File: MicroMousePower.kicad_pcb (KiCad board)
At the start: 2 copper layers, 103 parts, among them J1 USB_C_Receptacle_PowerOnly_6P, J2 Conn_02x16_Odd_Even, J3 Conn_01x02_Pin, Q1 TIP41C, Q2 TIP41C, Q3 TIP41C, U1 INA219AxDCN, U2 MCP73831-3-MC, U3 CH224K, U4 DRV8833PWPR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

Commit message: try 2
try ?
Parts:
- moved D1 144.7 mm to (259.3, 51.6), turned to -90 degrees
- moved C15 130.1 mm to (248.5, 88.1), turned to 180 degrees
- moved C8 129.2 mm to (248.5, 91.4), turned to 180 degrees
- moved D2 128.2 mm to (248.0, 72.2), turned to -90 degrees
- moved R36 125.9 mm to (264.2, 112.9), turned to -90 degrees
- moved R19 124.8 mm to (256.8, 47.8), turned to 180 degrees
- moved R21 124.7 mm to (251.7, 47.8), turned to 180 degrees
- moved R25 124.6 mm to (258.2, 74.7)
- moved R12 121.9 mm to (252.0, 120.1)
- moved R26 121.5 mm to (263.1, 74.7)
- moved U8 120.9 mm to (250.7, 107.8)
- moved R38 118.0 mm to (258.7, 111.6), turned to 90 degrees
- moved R20 117.8 mm to (259.3, 58.9), turned to -90 degrees
- moved TP8 117.4 mm to (266.1, 102.7)
- moved R41 117.2 mm to (251.8, 126.3)
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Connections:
- TP18 pad 1: unconnected-(TP18-Pad1) -> /3V3
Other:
- board text added: "Vc"
- board text added: "Ve"

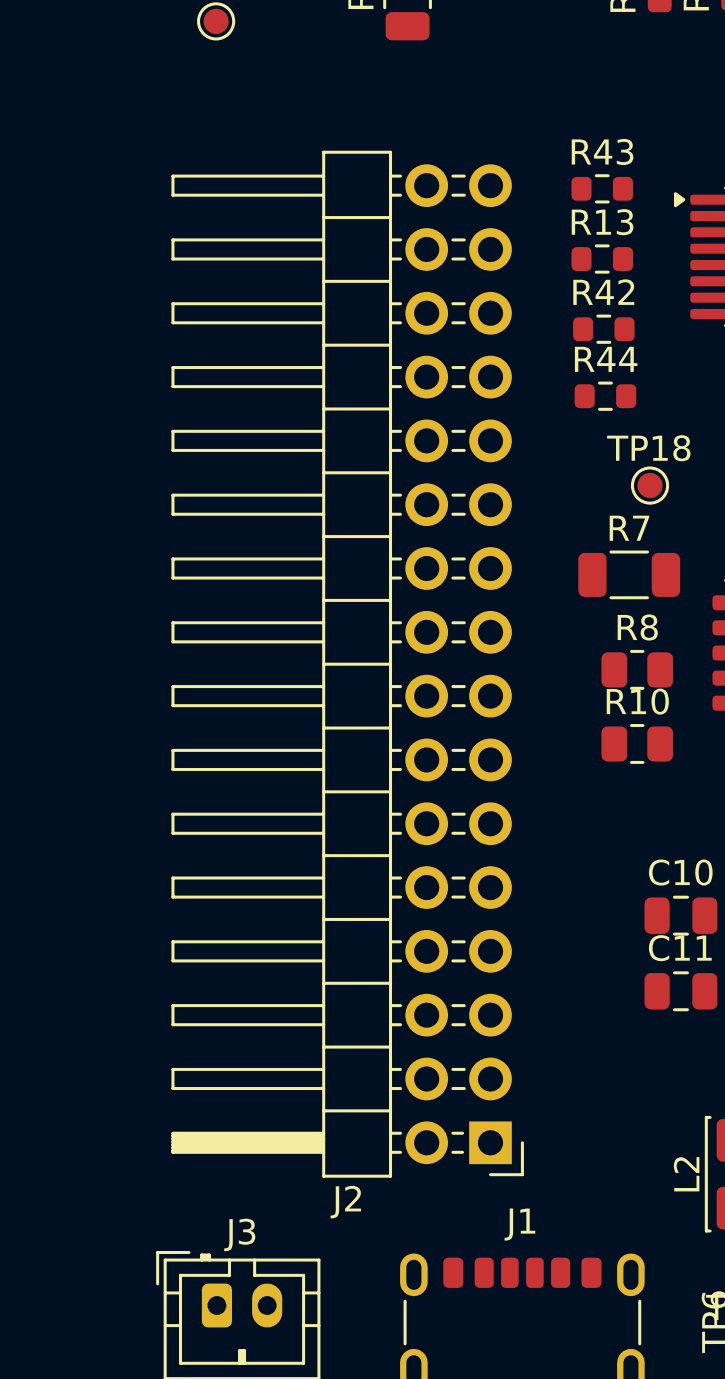
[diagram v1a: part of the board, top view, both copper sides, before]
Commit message: updated pinheader footprint
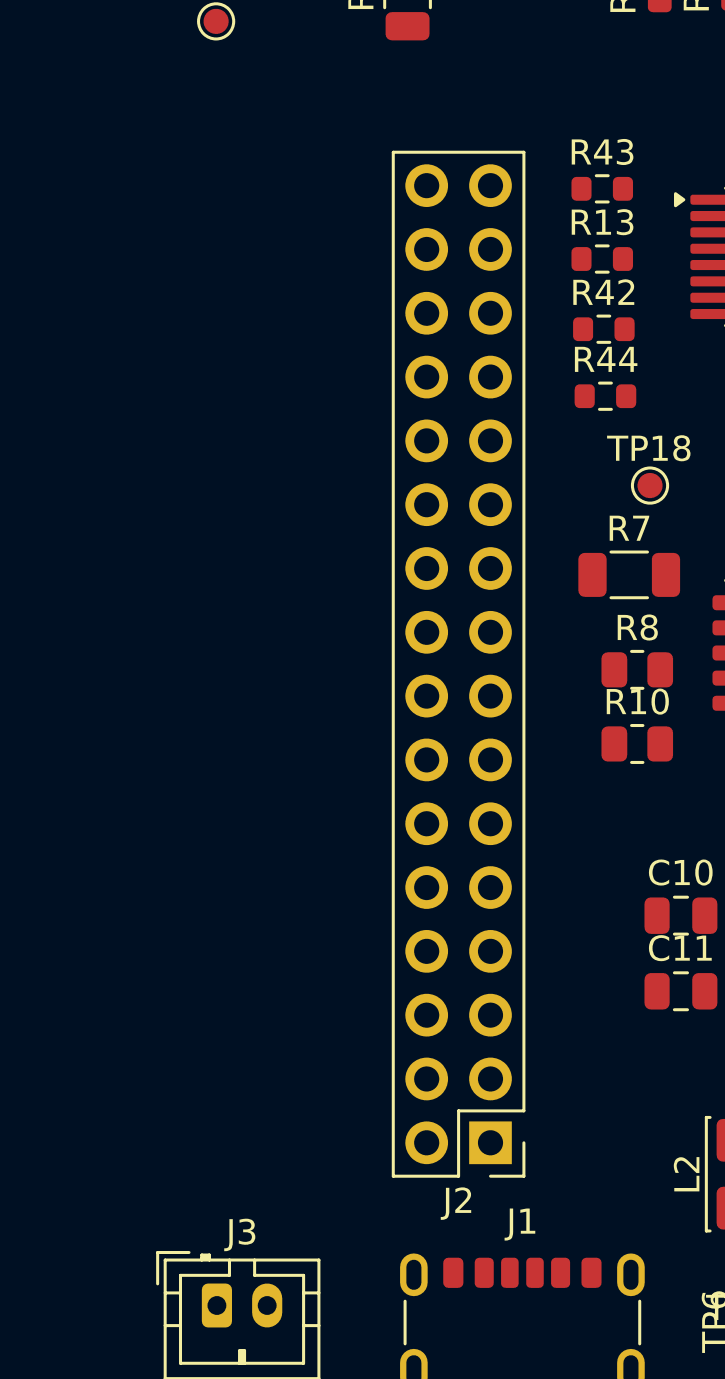
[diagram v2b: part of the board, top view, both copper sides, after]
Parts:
- J2: footprint Connector_PinHeader_2.54mm:PinHeader_2x16_P2.54mm_Horizontal -> Connector_PinHeader_2.54mm:PinHeader_2x16_P2.54mm_Vertical

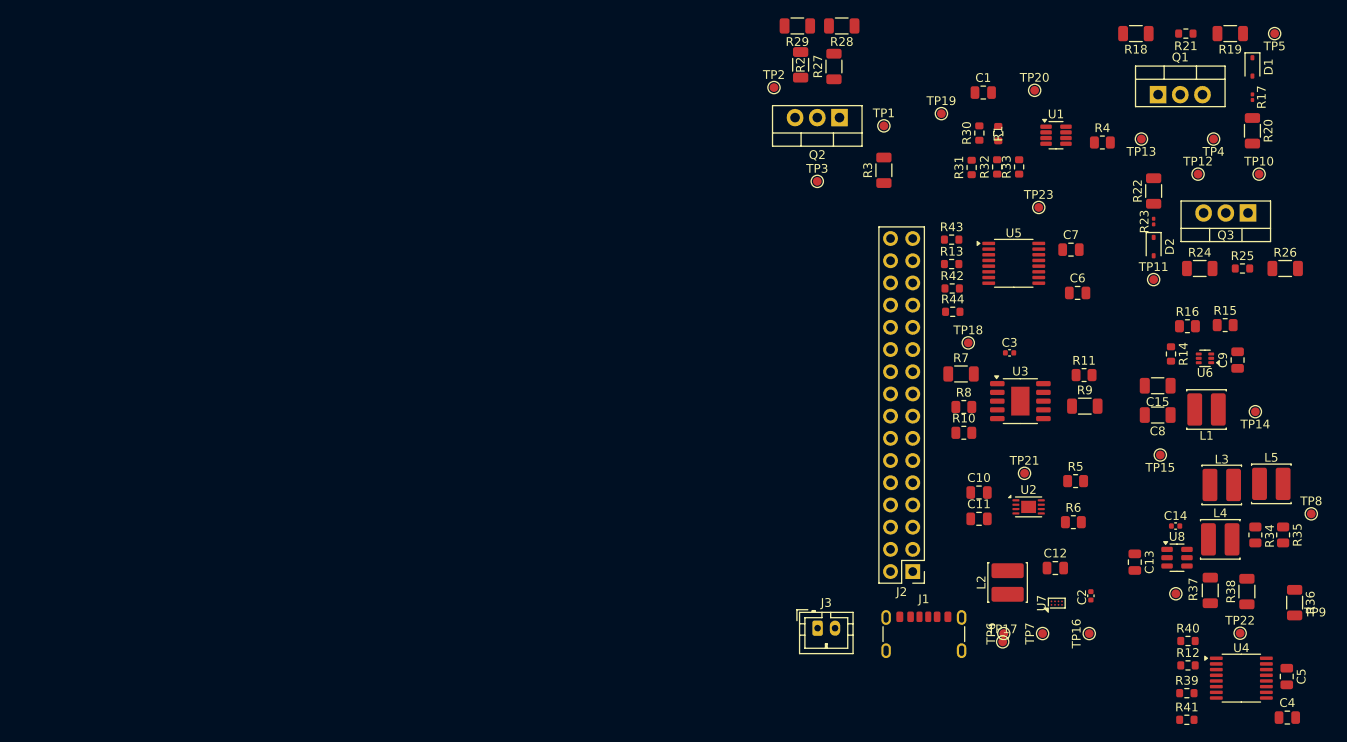
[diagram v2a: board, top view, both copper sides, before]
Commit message: rearranged pcb layout
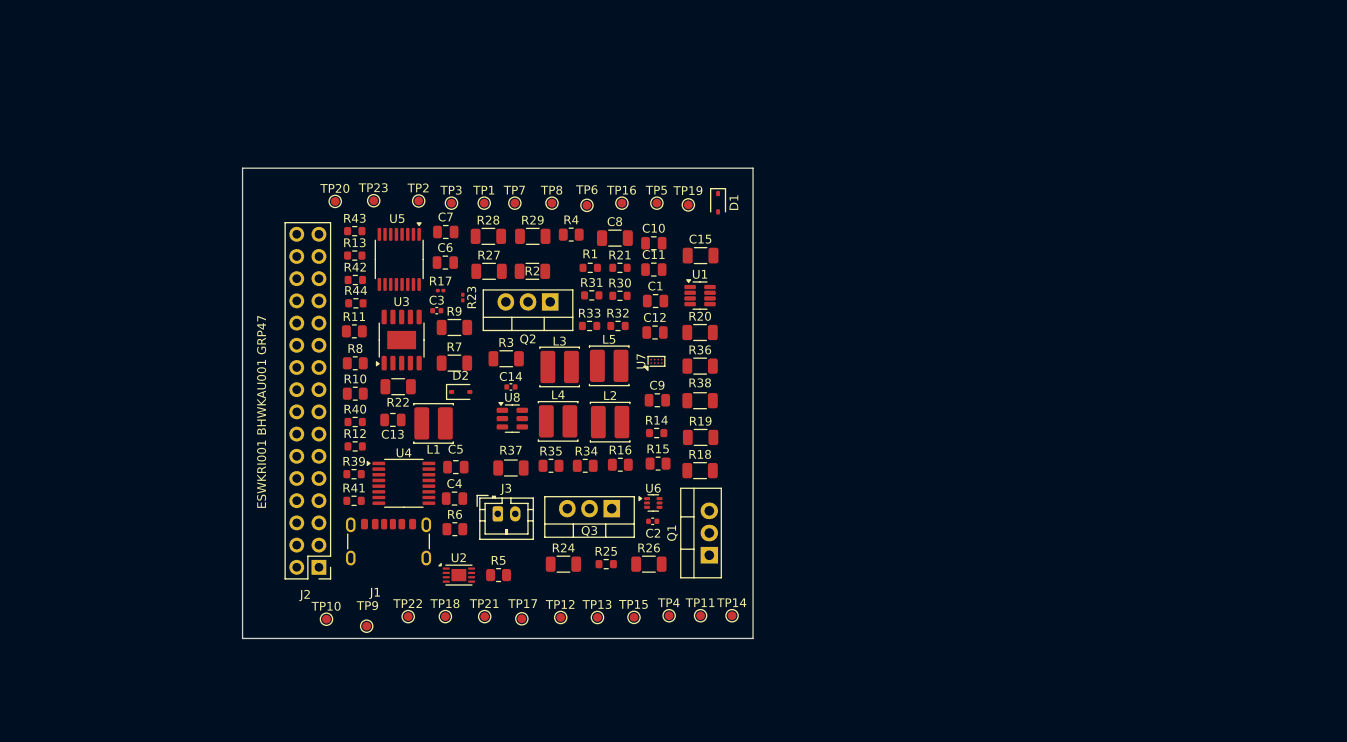
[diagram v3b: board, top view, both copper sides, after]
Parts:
- moved TP10 118.2 mm to (153.4, 114.8)
- moved C4 98.5 mm to (168.1, 101.0)
- moved R39 98.5 mm to (156.6, 98.2)
- moved R41 98.5 mm to (156.6, 101.3)
- moved R12 98.5 mm to (156.7, 95.0)
- moved R40 98.5 mm to (156.7, 92.2)
- moved U4 98.4 mm to (162.2, 99.2)
- moved C5 98.0 mm to (168.2, 97.4), turned to 0 degrees
- moved R17 95.5 mm to (166.5, 77.2), turned to 0 degrees
- moved TP22 95.2 mm to (162.8, 114.5)
- moved TP8 93.9 mm to (179.2, 67.2)
- moved TP9 92.6 mm to (158.0, 115.6), turned to 90 degrees
- moved R22 89.3 mm to (161.6, 88.2), turned to 180 degrees
- moved TP12 88.8 mm to (180.2, 114.6)
- moved L1 88.4 mm to (165.7, 92.4)
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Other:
- board outline added: 58.4 x 53.8 mm
- board text added: "ESWKRI001 BHWKAU001 GRP47"

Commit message: moved tips
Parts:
- moved R36 22.5 mm to (174.1, 81.4)
- moved R38 18.2 mm to (185.5, 104.6)
- moved R18 17.2 mm to (180.3, 104.6)
- moved R19 17.2 mm to (180.4, 100.8)
- moved R20 17.0 mm to (179.2, 81.2)
- moved Q2 16.3 mm to (195.3, 79.7), turned to -90 degrees
- moved Q3 12.6 mm to (197.0, 95.9), turned to 90 degrees
- moved C15 2.83 mm to (195.5, 70.5)
- moved U1 2.79 mm to (195.7, 75.0)
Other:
- board text added: "meow"
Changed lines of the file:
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@@
 	(footprint "Package_TO_SOT_THT:TO-220-3_Vertical"
 		(layer "F.Cu")
-		(at 186.035 102.15 180)
+		(at 197 95.88 90)
 		(descr "TO-220-3, Vertical, RM 2.54mm, see https://www.vishay.com/docs/66542/to-220-1.pdf")
 		(tags "TO-220-3 Vertical RM 2.54mm")
 		(property "Reference" "Q3"
-			(at 2.54 -2.54 0)
+			(at 2.54 -2.54 90)
 			(layer "F.SilkS")
 			(effects
@@
 		)
 		(property "Value" "TIP41C"
-			(at 2.54 2.5 0)
+			(at 2.54 2.5 90)
 			(layer "F.Fab")
 			(effects
@@
 		)
 		(property "Datasheet" "https://www.centralsemi.com/get_document.php?cmp=1&mergetype=pd&mergepath=pd&pdf_id=tip41.PDF"
-			(at 0 0 0)
+			(at 0 0 90)
 			(layer "F.Fab")
 			(hide yes)
@@
 		)
 		(property "Description" "6A Ic, 100V Vce, Power NPN Transistor, TO-220"
-			(at 0 0 0)
+			(at 0 0 90)
 			(layer "F.Fab")
 			(hide yes)
@@
 		)
 		(property "LCSC" "C92603"
-			(at 0 0 180)
+			(at 0 0 90)
 			(unlocked yes)
 			(layer "F.Fab")
@@
 		)
 		(fp_line
-			(start -2.58 1.371)
-			(end 7.66 1.371)
+			(start -2.58 -3.27)
+			(end 7.66 -3.27)
 			(stroke
 				(width 0.12)
@@
 		)
 		(fp_line
-			(start -2.58 -1.76)
-			(end 7.66 -1.76)
+			(start -2.58 -3.27)
+			(end -2.58 1.371)
 			(stroke
 				(width 0.12)
@@
 		)
 		(fp_line
-			(start -2.58 -3.27)
-			(end 7.66 -3.27)
+			(start -2.58 -1.76)
+			(end 7.66 -1.76)
 			(stroke
 				(width 0.12)
@@
 		)
 		(fp_line
-			(start -2.58 -3.27)
-			(end -2.58 1.371)
+			(start -2.58 1.371)
+			(end 7.66 1.371)
 			(stroke
 				(width 0.12)
@@
 		)
 		(fp_line
-			(start 7.79 1.51)
-			(end 7.79 -3.4)
-			(stroke
-				(width 0.05)
-				(type solid)
-			)
-			(layer "F.CrtYd")
-		)
-		(fp_line
 			(start 7.79 -3.4)
 			(end -2.71 -3.4)
@@
 		)
 		(fp_line
-			(start -2.71 1.51)
-			(end 7.79 1.51)
+			(start -2.71 -3.4)
+			(end -2.71 1.51)
 			(stroke
 				(width 0.05)
@@
 		)
 		(fp_line
-			(start -2.71 -3.4)
-			(end -2.71 1.51)
+			(start 7.79 1.51)
+			(end 7.79 -3.4)
 			(stroke
 				(width 0.05)
@@
 		)
 		(fp_line
-			(start 7.54 1.25)
-			(end 7.54 -3.15)
+			(start -2.71 1.51)
+			(end 7.79 1.51)
 			(stroke
-				(width 0.1)
+				(width 0.05)
 				(type solid)
 			)
-			(layer "F.Fab")
+			(layer "F.CrtYd")
 		)
 		(fp_line
@@
 		)
 		(fp_line
-			(start -2.46 1.25)
-			(end 7.54 1.25)
+			(start -2.46 -3.15)
+			(end -2.46 1.25)
 			(stroke
 				(width 0.1)
@@
 		)
 		(fp_line
-			(start -2.46 -3.15)
-			(end -2.46 1.25)
+			(start 7.54 1.25)
+			(end 7.54 -3.15)
+			(stroke
+				(width 0.1)
+				(type solid)
+			)
+			(layer "F.Fab")
+		)
+		(fp_line
+			(start -2.46 1.25)
+			(end 7.54 1.25)
 			(stroke
 				(width 0.1)
@@
 		)
 		(fp_text user "${REFERENCE}"
-			(at 2.54 -2.54 0)
+			(at 2.54 -2.54 90)
 			(layer "F.Fab")
 			(effects
@@
 		)
 		(pad "1" thru_hole rect
-			(at 0 0 180)
+			(at 0 0 90)
 			(size 1.905 2)
 			(drill 1.1)
@@
 		)
 		(pad "2" thru_hole oval
-			(at 2.54 0 180)
+			(at 2.54 0 90)
 			(size 1.905 2)
 			(drill 1.1)
@@
 		)
 		(pad "3" thru_hole oval
-			(at 5.08 0 180)
+			(at 5.08 0 90)
 			(size 1.905 2)
 			(drill 1.1)
@@
 	(footprint "Resistor_SMD:R_1206_3216Metric"
 		(layer "F.Cu")
-		(at 196.1465 85.8435)
+		(at 174.1375 81.4)
 		(descr "Resistor SMD 1206 (3216 Metric), square (rectangular) end terminal, IPC_7351 nominal, (Body size source: IPC-SM-782 page 72, https://www.pcb-3d.com/wordpress/wp-content/uploads/ipc-sm-782a_amendment_1_and_2.pdf), generated with kicad-footprint-generator")
 		(tags "resistor")
@@
 	(footprint "Resistor_SMD:R_1206_3216Metric"
 		(layer "F.Cu")
-		(at 196.1375 82)
+		(at 179.2 81.2)
 		(descr "Resistor SMD 1206 (3216 Metric), square (rectangular) end terminal, IPC_7351 nominal, (Body size source: IPC-SM-782 page 72, https://www.pcb-3d.com/wordpress/wp-content/uploads/ipc-sm-782a_amendment_1_and_2.pdf), generated with kicad-footprint-generator")
 		(tags "resistor")
@@
 	(footprint "Resistor_SMD:R_1206_3216Metric"
 		(layer "F.Cu")
-		(at 196.2 94)
+		(at 180.4 100.8)
 		(descr "Resistor SMD 1206 (3216 Metric), square (rectangular) end terminal, IPC_7351 nominal, (Body size source: IPC-SM-782 page 72, https://www.pcb-3d.com/wordpress/wp-content/uploads/ipc-sm-782a_amendment_1_and_2.pdf), generated with kicad-footprint-generator")
 		(tags "resistor")
@@
 	(footprint "Resistor_SMD:R_1206_3216Metric"
 		(layer "F.Cu")
-		(at 196.1375 97.8)
+		(at 180.3375 104.6)
 		(descr "Resistor SMD 1206 (3216 Metric), square (rectangular) end terminal, IPC_7351 nominal, (Body size source: IPC-SM-782 page 72, https://www.pcb-3d.com/wordpress/wp-content/uploads/ipc-sm-782a_amendment_1_and_2.pdf), generated with kicad-footprint-generator")
 		(tags "resistor")
@@
 	(footprint "Resistor_SMD:R_1206_3216Metric"
 		(layer "F.Cu")
-		(at 196.1375 89.8 180)
+		(at 185.5375 104.6 180)
 		(descr "Resistor SMD 1206 (3216 Metric), square (rectangular) end terminal, IPC_7351 nominal, (Body size source: IPC-SM-782 page 72, https://www.pcb-3d.com/wordpress/wp-content/uploads/ipc-sm-782a_amendment_1_and_2.pdf), generated with kicad-footprint-generator")
 		(tags "resistor")
@@
 	(footprint "Package_TO_SOT_SMD:SOT-23-8"
 		(layer "F.Cu")
-		(at 196.1375 77.775)
+		(at 195.6625 75.025)
 		(descr "SOT, 8 Pin (JEDEC MO-178 Var BA https://www.jedec.org/document_search?search_api_views_fulltext=MO-178), generated with kicad-footprint-generator ipc_gullwing_generator.py")
 		(tags "SOT TO_SOT_SMD")
@@
 	(footprint "Package_TO_SOT_THT:TO-220-3_Vertical"
 		(layer "F.Cu")
-		(at 179 78.5 180)
+		(at 195.255 79.66 -90)
 		(descr "TO-220-3, Vertical, RM 2.54mm, see https://www.vishay.com/docs/66542/to-220-1.pdf")
 		(tags "TO-220-3 Vertical RM 2.54mm")
 		(property "Reference" "Q2"
-			(at 2.54 -4.27 0)
+			(at 2.54 -4.27 90)
 			(layer "F.SilkS")
 			(effects
@@
 		)
 		(property "Value" "TIP41C"
-			(at 2.54 2.5 0)
+			(at 2.54 2.5 90)
 			(layer "F.Fab")
 			(effects
@@
 		)
 		(property "Datasheet" "https://www.centralsemi.com/get_document.php?cmp=1&mergetype=pd&mergepath=pd&pdf_id=tip41.PDF"
-			(at 0 0 0)
+			(at 0 0 90)
 			(layer "F.Fab")
 			(hide yes)
@@
 		)
 		(property "Description" "6A Ic, 100V Vce, Power NPN Transistor, TO-220"
-			(at 0 0 0)
+			(at 0 0 90)
 			(layer "F.Fab")
 			(hide yes)
@@
 		)
 		(property "LCSC" "C92603"
-			(at 0 0 180)
+			(at 0 0 270)
 			(unlocked yes)
 			(layer "F.Fab")
@@
 		(attr through_hole)
 		(fp_line
-			(start 7.66 -3.27)
+			(start -2.58 1.371)
 			(end 7.66 1.371)
 			(stroke
@@
 		)
 		(fp_line
-			(start 4.391 -3.27)
-			(end 4.391 -1.76)
+			(start -2.58 -1.76)
+			(end 7.66 -1.76)
 			(stroke
 				(width 0.12)
@@
 		)
 		(fp_line
-			(start 0.69 -3.27)
-			(end 0.69 -1.76)
+			(start -2.58 -3.27)
+			(end -2.58 1.371)
 			(stroke
 				(width 0.12)
@@
 		)
 		(fp_line
-			(start -2.58 1.371)
-			(end 7.66 1.371)
+			(start -2.58 -3.27)
+			(end 7.66 -3.27)
 			(stroke
 				(width 0.12)
@@
 		)
 		(fp_line
-			(start -2.58 -1.76)
-			(end 7.66 -1.76)
+			(start 0.69 -3.27)
+			(end 0.69 -1.76)
 			(stroke
 				(width 0.12)
@@
 		)
 		(fp_line
-			(start -2.58 -3.27)
-			(end 7.66 -3.27)
+			(start 4.391 -3.27)
+			(end 4.391 -1.76)
 			(stroke
 				(width 0.12)
@@
 		)
 		(fp_line
-			(start -2.58 -3.27)
-			(end -2.58 1.371)
+			(start 7.66 -3.27)
+			(end 7.66 1.371)
 			(stroke
 				(width 0.12)
@@
 		)
 		(fp_line
-			(start 7.79 1.51)
-			(end 7.79 -3.4)
+			(start -2.71 1.51)
+			(end 7.79 1.51)
 			(stroke
 				(width 0.05)
@@
 		)
 		(fp_line
-			(start 7.79 -3.4)
-			(end -2.71 -3.4)
+			(start 7.79 1.51)
+			(end 7.79 -3.4)
 			(stroke
 				(width 0.05)
@@
 		)
 		(fp_line
-			(start -2.71 1.51)
-			(end 7.79 1.51)
+			(start -2.71 -3.4)
+			(end -2.71 1.51)
 			(stroke
 				(width 0.05)
@@
 		)
 		(fp_line
-			(start -2.71 -3.4)
-			(end -2.71 1.51)
+			(start 7.79 -3.4)
+			(end -2.71 -3.4)
 			(stroke
 				(width 0.05)
@@
 		)
 		(fp_line
-			(start 7.54 1.25)
-			(end 7.54 -3.15)
+			(start -2.46 1.25)
+			(end 7.54 1.25)
 			(stroke
 				(width 0.1)
@@
 		)
 		(fp_line
-			(start 7.54 -3.15)
-			(end -2.46 -3.15)
+			(start 7.54 1.25)
+			(end 7.54 -3.15)
 			(stroke
 				(width 0.1)
@@
 		)
 		(fp_line
-			(start 4.39 -3.15)
-			(end 4.39 -1.88)
+			(start -2.46 -1.88)
+			(end 7.54 -1.88)
 			(stroke
 				(width 0.1)
@@
 		)
 		(fp_line
-			(start 0.69 -3.15)
-			(end 0.69 -1.88)
+			(start -2.46 -3.15)
+			(end -2.46 1.25)
 			(stroke
 				(width 0.1)
@@
 		)
 		(fp_line
-			(start -2.46 1.25)
-			(end 7.54 1.25)
+			(start 0.69 -3.15)
+			(end 0.69 -1.88)
 			(stroke
 				(width 0.1)
@@
 		)
 		(fp_line
-			(start -2.46 -1.88)
-			(end 7.54 -1.88)
+			(start 4.39 -3.15)
+			(end 4.39 -1.88)
 			(stroke
 				(width 0.1)
@@
 		)
 		(fp_line
-			(start -2.46 -3.15)
-			(end -2.46 1.25)
+			(start 7.54 -3.15)
+			(end -2.46 -3.15)
 			(stroke
 				(width 0.1)
@@
 		)
 		(fp_text user "${REFERENCE}"
-			(at 2.54 -4.27 0)
+			(at 2.54 -4.27 90)
 			(layer "F.Fab")
 			(effects
@@
 		)
 		(pad "1" thru_hole rect
-			(at 0 0 180)
+			(at 0 0 270)
 			(size 1.905 2)
 			(drill 1.1)
@@
 		)
 		(pad "2" thru_hole oval
-			(at 2.54 0 180)
+			(at 2.54 0 270)
 			(size 1.905 2)
 			(drill 1.1)
@@
 		)
 		(pad "3" thru_hole oval
-			(at 5.08 0 180)
+			(at 5.08 0 270)
 			(size 1.905 2)
 			(drill 1.1)
@@
 	(footprint "Capacitor_SMD:C_1206_3216Metric"
 		(layer "F.Cu")
-		(at 196.2 73.2)
+		(at 195.525 70.45)
 		(descr "Capacitor SMD 1206 (3216 Metric), square (rectangular) end terminal, IPC_7351 nominal, (Body size source: IPC-SM-782 page 76, https://www.pcb-3d.com/wordpress/wp-content/uploads/ipc-sm-782a_amendment_1_and_2.pdf), generated with kicad-footprint-generator")
 		(tags "capacitor")
 		(property "Reference" "C15"
-			(at 0 -1.85 0)
+			(at 3.475 0.15 90)
 			(layer "F.SilkS")
 			(effects
@@
 		(layer "F.SilkS")
 		(effects
+			(font
+				(size 1 1)
+				(thickness 0.1)
+			)
+			(justify left bottom)
+		)
+	)
+	(gr_text "meow"
+		(at 149.4 68.8 0)
+		(layer "F.SilkS")
+		(effects
